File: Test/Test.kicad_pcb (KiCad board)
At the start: 2 copper layers, 43 x 65 mm, 4 parts, among them J1 Conn_01x20, J2 Conn_01x20, J3 Conn_01x03, U1 Pico

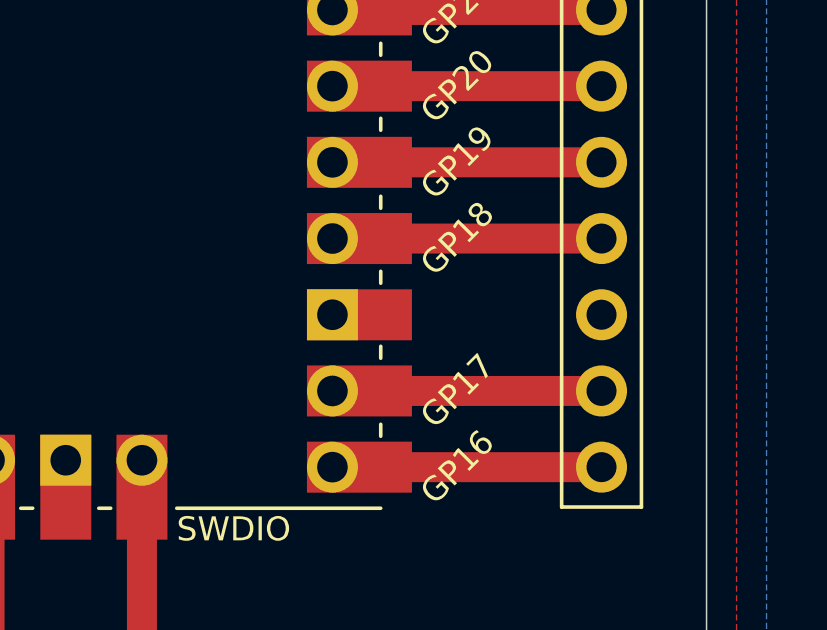
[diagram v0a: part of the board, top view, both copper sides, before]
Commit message: Updated footprints to their correct types -  Updated 'Test' project to use updated footprint
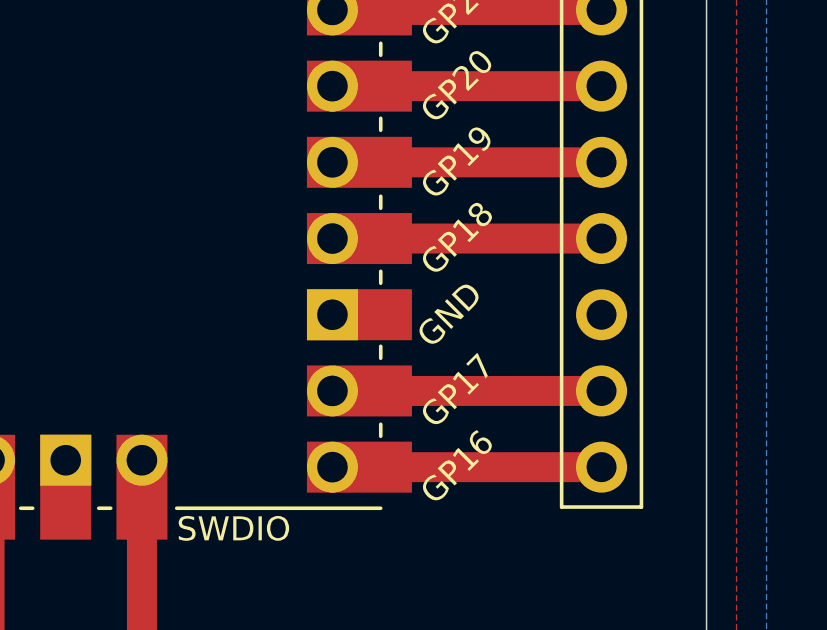
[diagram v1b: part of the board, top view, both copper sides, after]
